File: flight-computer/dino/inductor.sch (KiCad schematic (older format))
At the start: 3 parts

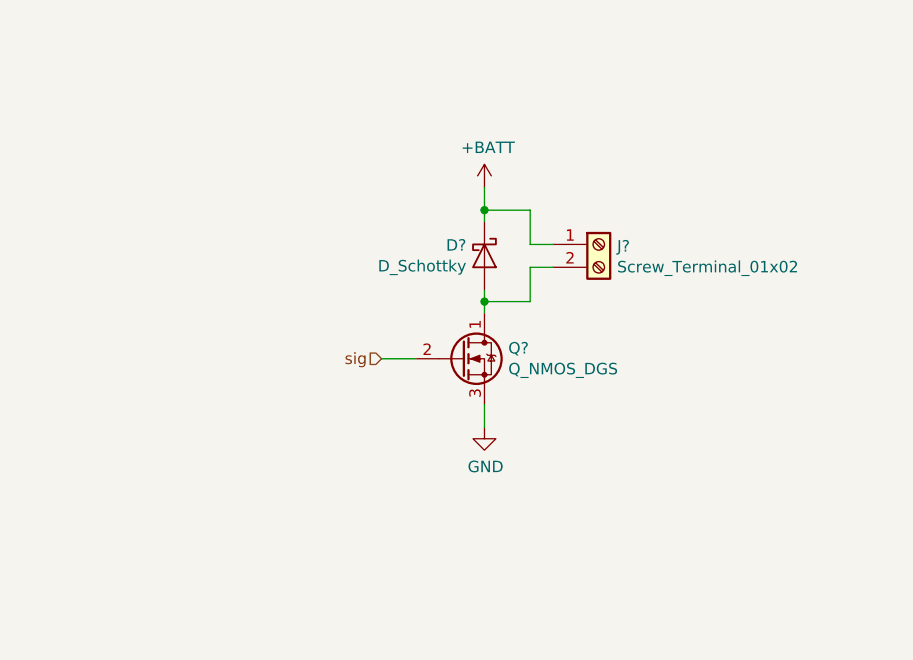
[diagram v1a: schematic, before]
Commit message: fc schematic fleshing-out and mcu docs
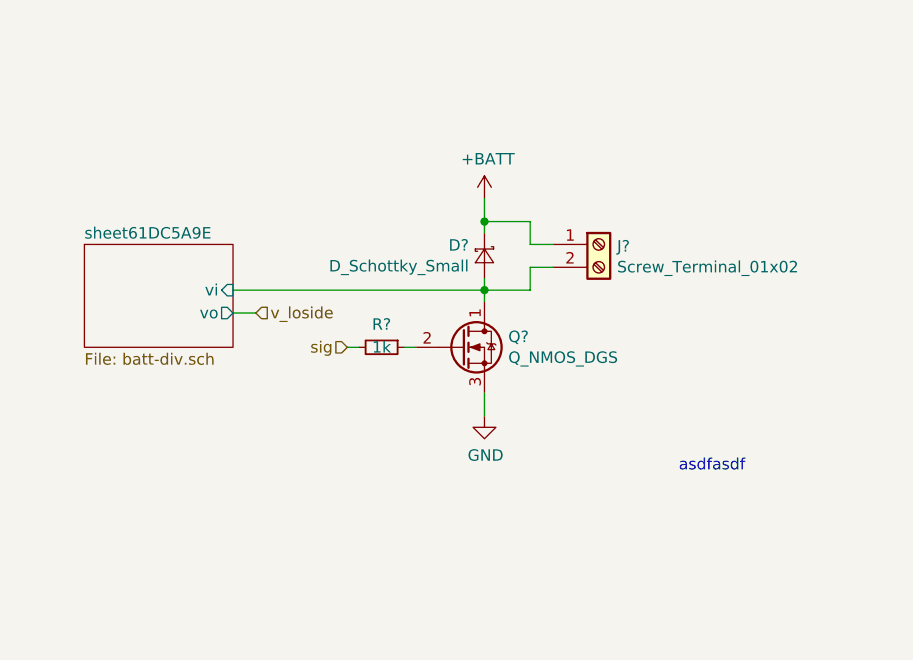
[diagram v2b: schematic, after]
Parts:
- removed D?: D_Schottky, symbol Device:D_Schottky
- added D?: D_Schottky_Small, symbol Device:D_Schottky_Small
- added R?: 1k, symbol Device:R_Small
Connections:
- net +BATT: now also D?.1 (K)
- net sig: now also R?.2; no longer Q?.2 (G)
- net sheet61DC5A9E/vi: now reaches J?.2 (Pin_2), Q?.1 (D)
- net sheet61DC5A9E/vi: now also D?.2 (A)
- new net: Q?.2 (G), R?.1
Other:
- note added: "asdfasdf"
- moved on the sheet: Q?
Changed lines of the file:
@@
 $Descr A 11000 8500
 encoding utf-8
-Sheet 2 8
+Sheet 10 14
 Title ""
 Date ""
@@
 L Device:Q_NMOS_DGS Q?
 U 1 1 61C15CF4
-P 5250 4600
+P 5250 4550
 AR Path="/61C15AA8/61C15CF4" Ref="Q?"  Part="1"
 AR Path="/61C229AC/61C15CF4" Ref="Q?"  Part="1"
 AR Path="/61C27E7D/61C15CF4" Ref="Q?"  Part="1"
 AR Path="/61C27F52/61C15CF4" Ref="Q?"  Part="1"
-F 0 "Q?" H 5454 4646 50  0000 L CNN
-F 1 "Q_NMOS_DGS" H 5454 4555 50  0000 L CNN
-F 2 "" H 5450 4700 50  0001 C CNN
-F 3 "~" H 5250 4600 50  0001 C CNN
-	1    5250 4600
+AR Path="/61D7382A/61C15CF4" Ref="Q?"  Part="1"
+F 0 "Q?" H 5454 4596 50  0000 L CNN
+F 1 "Q_NMOS_DGS" H 5454 4505 50  0000 L CNN
+F 2 "" H 5450 4650 50  0001 C CNN
+F 3 "~" H 5250 4550 50  0001 C CNN
+	1    5250 4550
 	1    0    0    -1
 $EndComp
@@
 L power:+BATT #PWR?
 U 1 1 61C163F4
-P 5350 3850
+P 5350 3900
 AR Path="/61C15AA8/61C163F4" Ref="#PWR?"  Part="1"
 AR Path="/61C229AC/61C163F4" Ref="#PWR?"  Part="1"
 AR Path="/61C27E7D/61C163F4" Ref="#PWR?"  Part="1"
 AR Path="/61C27F52/61C163F4" Ref="#PWR?"  Part="1"
-F 0 "#PWR?" H 5350 3700 50  0001 C CNN
-F 1 "+BATT" H 5365 4023 50  0000 C CNN
-F 2 "" H 5350 3850 50  0001 C CNN
-F 3 "" H 5350 3850 50  0001 C CNN
-	1    5350 3850
+AR Path="/61D7382A/61C163F4" Ref="#PWR?"  Part="1"
+F 0 "#PWR?" H 5350 3750 50  0001 C CNN
+F 1 "+BATT" H 5365 4073 50  0000 C CNN
+F 2 "" H 5350 3900 50  0001 C CNN
+F 3 "" H 5350 3900 50  0001 C CNN
+	1    5350 3900
 	1    0    0    -1
 $EndComp
@@
 L power:GND #PWR?
 U 1 1 61C16FAC
-P 5350 4900
+P 5350 4850
 AR Path="/61C15AA8/61C16FAC" Ref="#PWR?"  Part="1"
 AR Path="/61C229AC/61C16FAC" Ref="#PWR?"  Part="1"
 AR Path="/61C27E7D/61C16FAC" Ref="#PWR?"  Part="1"
 AR Path="/61C27F52/61C16FAC" Ref="#PWR?"  Part="1"
-F 0 "#PWR?" H 5350 4650 50  0001 C CNN
-F 1 "GND" H 5355 4727 50  0000 C CNN
-F 2 "" H 5350 4900 50  0001 C CNN
-F 3 "" H 5350 4900 50  0001 C CNN
-	1    5350 4900
+AR Path="/61D7382A/61C16FAC" Ref="#PWR?"  Part="1"
+F 0 "#PWR?" H 5350 4600 50  0001 C CNN
+F 1 "GND" H 5355 4677 50  0000 C CNN
+F 2 "" H 5350 4850 50  0001 C CNN
+F 3 "" H 5350 4850 50  0001 C CNN
+	1    5350 4850
 	1    0    0    -1
-$EndComp
-$Comp
-L Device:D_Schottky D?
-U 1 1 61C1778E
-P 5350 4150
-AR Path="/61C15AA8/61C1778E" Ref="D?"  Part="1"
-AR Path="/61C229AC/61C1778E" Ref="D?"  Part="1"
-AR Path="/61C27E7D/61C1778E" Ref="D?"  Part="1"
-AR Path="/61C27F52/61C1778E" Ref="D?"  Part="1"
-F 0 "D?" V 5304 4071 50  0000 R CNN
-F 1 "D_Schottky" V 5395 4071 50  0000 R CNN
-F 2 "" H 5350 4150 50  0001 C CNN
-F 3 "~" H 5350 4150 50  0001 C CNN
-	1    5350 4150
-	0    1    1    0
 $EndComp
 $Comp
@@
 AR Path="/61C27E7D/61C18064" Ref="J?"  Part="1"
 AR Path="/61C27F52/61C18064" Ref="J?"  Part="1"
+AR Path="/61D7382A/61C18064" Ref="J?"  Part="1"
 F 0 "J?" H 5930 4092 50  0000 L CNN
 F 1 "Screw_Terminal_01x02" H 5930 4001 50  0000 L CNN
@@
 $EndComp
 Wire Wire Line
-	5350 3850 5350 3950
+	5350 3900 5350 4000
 Wire Wire Line
 	5650 4100 5550 4100
 Wire Wire Line
-	5550 4100 5550 3950
+	5550 4000 5350 4000
+Connection ~ 5350 4000
 Wire Wire Line
-	5550 3950 5350 3950
-Connection ~ 5350 3950
+	5350 4000 5350 4050
 Wire Wire Line
-	5350 3950 5350 4000
+	5350 4250 5350 4300
+Wire Wire Line
+	5350 4300 5550 4300
+Wire Wire Line
+	5550 4300 5550 4200
+Wire Wire Line
+	5550 4200 5650 4200
+Connection ~ 5350 4300
 Wire Wire Line
 	5350 4300 5350 4350
 Wire Wire Line
-	5350 4350 5550 4350
+	5350 4750 5350 4850
+Text HLabel 4750 4550 0    50   Input ~ 0
+sig
+$Sheet
+S 3600 4100 650  450
+U 61DC5AA2
+F0 "sheet61DC5A9E" 50
+F1 "batt-div.sch" 50
+F2 "vo" O R 4250 4400 50
+F3 "vi" I R 4250 4300 50
+$EndSheet
 Wire Wire Line
-	5550 4350 5550 4200
+	5350 4300 4250 4300
 Wire Wire Line
-	5550 4200 5650 4200
-Connection ~ 5350 4350
+	4250 4400 4350 4400
+Text HLabel 4350 4400 2    50   Input ~ 0
+v_loside
+$Comp
+L Device:R_Small R?
+U 1 1 61DCB57D
+P 4900 4550
+AR Path="/61C27E7D/61DCB57D" Ref="R?"  Part="1"
+AR Path="/61C27F52/61DCB57D" Ref="R?"  Part="1"
+F 0 "R?" V 4800 4550 50  0000 C CNN
+F 1 "1k" V 4900 4550 50  0000 C CNN
+F 2 "" H 4900 4550 50  0001 C CNN
+F 3 "~" H 4900 4550 50  0001 C CNN
+	1    4900 4550
+	0    1    1    0
+$EndComp
+$Comp
+L Device:D_Schottky_Small D?
+U 1 1 61DCC192
+P 5350 4150
+AR Path="/61C27E7D/61DCC192" Ref="D?"  Part="1"
+AR Path="/61C27F52/61DCC192" Ref="D?"  Part="1"
+F 0 "D?" V 5304 4082 50  0000 R CNN
+F 1 "D_Schottky_Small" V 5395 4082 50  0000 R CNN
+F 2 "" V 5350 4150 50  0001 C CNN
+F 3 "~" V 5350 4150 50  0001 C CNN
+	1    5350 4150
+	0    1    1    0
+$EndComp
 Wire Wire Line
-	5350 4350 5350 4400
+	5550 4100 5550 4000
 Wire Wire Line
-	5350 4800 5350 4900
+	4750 4550 4800 4550
 Wire Wire Line
-	5050 4600 4900 4600
-Text HLabel 4900 4600 0    50   Input ~ 0
-sig
+	5000 4550 5050 4550
+Text Notes 6200 5100 0    50   ~ 0
+asdfasdf
 $EndSCHEMATC

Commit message: fc pinout and component selection. general cleanup
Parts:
- removed Q?: Q_NMOS_DGS, symbol Device:Q_NMOS_DGS
- added C?: 10u, Capacitor_Tantalum_SMD:CP_EIA-3216-18_Kemet-A, symbol Device:CP1
- added Q?: AO3400A, Package_TO_SOT_SMD:SOT-23, symbol Device:Q_NMOS_GSD
- added SW?: SW_SPDT, Connector_PinHeader_2.54mm:PinHeader_1x03_P2.54mm_Vertical, symbol Switch:SW_SPDT
- added TP? (x2): TestPoint, TestPoint:TestPoint_Keystone_5010-5014_Multipurpose, symbol Connector:TestPoint
- D?: value D_Schottky_Small -> 40V 5A 550mV; footprint (none) -> Diode_SMD:D_SMA; LCSC (none) -> C22452
- R?: footprint (none) -> Resistor_SMD:R_0603_1608Metric; LCSC (none) -> C21190
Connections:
- net labels added: v_hiside, v_sens_loside
- net labels removed: v_loside
- wire segments 15 -> 27
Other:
- note added: "LAYOUT: cap must be near connector"
- note added: "WARN: v_hiside can exceed 12V!"
- note added: "arming switch"
- note added: "decoupling cap"
- note removed: "asdfasdf"
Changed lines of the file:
@@
 $Descr A 11000 8500
 encoding utf-8
-Sheet 10 14
+Sheet 9 14
 Title ""
 Date ""
@@
 $EndDescr
 $Comp
-L Device:Q_NMOS_DGS Q?
-U 1 1 61C15CF4
-P 5250 4550
-AR Path="/61C15AA8/61C15CF4" Ref="Q?"  Part="1"
-AR Path="/61C229AC/61C15CF4" Ref="Q?"  Part="1"
-AR Path="/61C27E7D/61C15CF4" Ref="Q?"  Part="1"
-AR Path="/61C27F52/61C15CF4" Ref="Q?"  Part="1"
-AR Path="/61D7382A/61C15CF4" Ref="Q?"  Part="1"
-F 0 "Q?" H 5454 4596 50  0000 L CNN
-F 1 "Q_NMOS_DGS" H 5454 4505 50  0000 L CNN
-F 2 "" H 5450 4650 50  0001 C CNN
-F 3 "~" H 5250 4550 50  0001 C CNN
-	1    5250 4550
-	1    0    0    -1
-$EndComp
-$Comp
 L power:+BATT #PWR?
 U 1 1 61C163F4
-P 5350 3900
+P 5250 3450
 AR Path="/61C15AA8/61C163F4" Ref="#PWR?"  Part="1"
 AR Path="/61C229AC/61C163F4" Ref="#PWR?"  Part="1"
@@
 AR Path="/61C27F52/61C163F4" Ref="#PWR?"  Part="1"
 AR Path="/61D7382A/61C163F4" Ref="#PWR?"  Part="1"
-F 0 "#PWR?" H 5350 3750 50  0001 C CNN
-F 1 "+BATT" H 5365 4073 50  0000 C CNN
-F 2 "" H 5350 3900 50  0001 C CNN
-F 3 "" H 5350 3900 50  0001 C CNN
-	1    5350 3900
+AR Path="/61F91E79/61C163F4" Ref="#PWR?"  Part="1"
+AR Path="/61F965DC/61C163F4" Ref="#PWR?"  Part="1"
+AR Path="/61F965E7/61C163F4" Ref="#PWR?"  Part="1"
+F 0 "#PWR?" H 5250 3300 50  0001 C CNN
+F 1 "+BATT" H 5265 3623 50  0000 C CNN
+F 2 "" H 5250 3450 50  0001 C CNN
+F 3 "" H 5250 3450 50  0001 C CNN
+	1    5250 3450
 	1    0    0    -1
 $EndComp
@@
 AR Path="/61C27F52/61C16FAC" Ref="#PWR?"  Part="1"
 AR Path="/61D7382A/61C16FAC" Ref="#PWR?"  Part="1"
+AR Path="/61F91E79/61C16FAC" Ref="#PWR?"  Part="1"
+AR Path="/61F965DC/61C16FAC" Ref="#PWR?"  Part="1"
+AR Path="/61F965E7/61C16FAC" Ref="#PWR?"  Part="1"
 F 0 "#PWR?" H 5350 4600 50  0001 C CNN
 F 1 "GND" H 5355 4677 50  0000 C CNN
@@
 AR Path="/61C27F52/61C18064" Ref="J?"  Part="1"
 AR Path="/61D7382A/61C18064" Ref="J?"  Part="1"
+AR Path="/61F91E79/61C18064" Ref="J?"  Part="1"
+AR Path="/61F965DC/61C18064" Ref="J?"  Part="1"
+AR Path="/61F965E7/61C18064" Ref="J?"  Part="1"
 F 0 "J?" H 5930 4092 50  0000 L CNN
 F 1 "Screw_Terminal_01x02" H 5930 4001 50  0000 L CNN
@@
 $EndComp
 Wire Wire Line
-	5350 3900 5350 4000
-Wire Wire Line
 	5650 4100 5550 4100
 Wire Wire Line
@@
 Wire Wire Line
 	5350 4750 5350 4850
-Text HLabel 4750 4550 0    50   Input ~ 0
+Text HLabel 4700 4550 0    50   Input ~ 0
 sig
 $Sheet
@@
 	5350 4300 4250 4300
 Wire Wire Line
-	4250 4400 4350 4400
+	4250 4400 4300 4400
 Text HLabel 4350 4400 2    50   Input ~ 0
-v_loside
+v_sens_loside
 $Comp
 L Device:R_Small R?
@@
 AR Path="/61C27E7D/61DCB57D" Ref="R?"  Part="1"
 AR Path="/61C27F52/61DCB57D" Ref="R?"  Part="1"
+AR Path="/61C15AA8/61DCB57D" Ref="R?"  Part="1"
+AR Path="/61F91E79/61DCB57D" Ref="R?"  Part="1"
+AR Path="/61F965DC/61DCB57D" Ref="R?"  Part="1"
+AR Path="/61F965E7/61DCB57D" Ref="R?"  Part="1"
 F 0 "R?" V 4800 4550 50  0000 C CNN
 F 1 "1k" V 4900 4550 50  0000 C CNN
-F 2 "" H 4900 4550 50  0001 C CNN
+F 2 "Resistor_SMD:R_0603_1608Metric" H 4900 4550 50  0001 C CNN
 F 3 "~" H 4900 4550 50  0001 C CNN
+F 4 "C21190" V 4900 4550 50  0001 C CNN "LCSC"
 	1    4900 4550
 	0    1    1    0
@@
 AR Path="/61C27E7D/61DCC192" Ref="D?"  Part="1"
 AR Path="/61C27F52/61DCC192" Ref="D?"  Part="1"
+AR Path="/61C15AA8/61DCC192" Ref="D?"  Part="1"
+AR Path="/61F91E79/61DCC192" Ref="D?"  Part="1"
+AR Path="/61F965DC/61DCC192" Ref="D?"  Part="1"
+AR Path="/61F965E7/61DCC192" Ref="D?"  Part="1"
 F 0 "D?" V 5304 4082 50  0000 R CNN
-F 1 "D_Schottky_Small" V 5395 4082 50  0000 R CNN
-F 2 "" V 5350 4150 50  0001 C CNN
-F 3 "~" V 5350 4150 50  0001 C CNN
+F 1 "40V 5A 550mV" V 5395 4082 50  0000 R CNN
+F 2 "Diode_SMD:D_SMA" V 5350 4150 50  0001 C CNN
+F 3 "https://datasheet.lcsc.com/lcsc/1810192041_MDD%EF%BC%88Microdiode-Electronics%EF%BC%89-SS54_C22452.pdf" V 5350 4150 50  0001 C CNN
+F 4 "C22452" V 5350 4150 50  0001 C CNN "LCSC"
 	1    5350 4150
 	0    1    1    0
@@
 Wire Wire Line
 	5000 4550 5050 4550
-Text Notes 6200 5100 0    50   ~ 0
-asdfasdf
+$Comp
+L Device:Q_NMOS_GSD Q?
+U 1 1 61E3754D
+P 5250 4550
+AR Path="/61C27F52/61E3754D" Ref="Q?"  Part="1"
+AR Path="/61C15AA8/61E3754D" Ref="Q?"  Part="1"
+AR Path="/61C27E7D/61E3754D" Ref="Q?"  Part="1"
+AR Path="/61F91E79/61E3754D" Ref="Q?"  Part="1"
+AR Path="/61F965DC/61E3754D" Ref="Q?"  Part="1"
+AR Path="/61F965E7/61E3754D" Ref="Q?"  Part="1"
+F 0 "Q?" H 5455 4596 50  0000 L CNN
+F 1 "AO3400A" H 5455 4505 50  0000 L CNN
+F 2 "Package_TO_SOT_SMD:SOT-23" H 5450 4650 50  0001 C CNN
+F 3 "https://datasheet.lcsc.com/lcsc/1811081213_Alpha-&-Omega-Semicon-AO3400A_C20917.pdf" H 5250 4550 50  0001 C CNN
+	1    5250 4550
+	1    0    0    -1
+$EndComp
+$Comp
+L power:+BATT #PWR?
+U 1 1 61E403DE
+P 3900 5050
+AR Path="/61C229AC/61E403DE" Ref="#PWR?"  Part="1"
+AR Path="/61C267AB/61E403DE" Ref="#PWR?"  Part="1"
+AR Path="/61C3727F/61E403DE" Ref="#PWR?"  Part="1"
+AR Path="/61C37282/61E403DE" Ref="#PWR?"  Part="1"
+AR Path="/61DB5304/61E403DE" Ref="#PWR?"  Part="1"
+AR Path="/61C15AA8/61E403DE" Ref="#PWR?"  Part="1"
+AR Path="/61C27F52/61E403DE" Ref="#PWR?"  Part="1"
+AR Path="/61C27E7D/61E403DE" Ref="#PWR?"  Part="1"
+AR Path="/61F91E79/61E403DE" Ref="#PWR?"  Part="1"
+AR Path="/61F965DC/61E403DE" Ref="#PWR?"  Part="1"
+AR Path="/61F965E7/61E403DE" Ref="#PWR?"  Part="1"
+F 0 "#PWR?" H 3900 4900 50  0001 C CNN
+F 1 "+BATT" H 3915 5223 50  0000 C CNN
+F 2 "" H 3900 5050 50  0001 C CNN
+F 3 "" H 3900 5050 50  0001 C CNN
+	1    3900 5050
+	1    0    0    -1
+$EndComp
+$Comp
+L power:GND #PWR?
+U 1 1 61E403EA
+P 3900 5450
+AR Path="/61C229AC/61E403EA" Ref="#PWR?"  Part="1"
+AR Path="/61C15AA8/61E403EA" Ref="#PWR?"  Part="1"
+AR Path="/61C27F52/61E403EA" Ref="#PWR?"  Part="1"
+AR Path="/61C27E7D/61E403EA" Ref="#PWR?"  Part="1"
+AR Path="/61F91E79/61E403EA" Ref="#PWR?"  Part="1"
+AR Path="/61F965DC/61E403EA" Ref="#PWR?"  Part="1"
+AR Path="/61F965E7/61E403EA" Ref="#PWR?"  Part="1"
+F 0 "#PWR?" H 3900 5200 50  0001 C CNN
+F 1 "GND" H 3905 5277 50  0000 C CNN
+F 2 "" H 3900 5450 50  0001 C CNN
+F 3 "" H 3900 5450 50  0001 C CNN
+	1    3900 5450
+	1    0    0    -1
+$EndComp
+Wire Wire Line
+	3900 5450 3900 5400
+Wire Wire Line
+	3900 5100 3900 5050
+Text Notes 3650 5750 0    50   ~ 0
+decoupling cap
+$Comp
+L Switch:SW_SPDT SW?
+U 1 1 61E69DDA
+P 5350 3700
+AR Path="/61C27E7D/61E69DDA" Ref="SW?"  Part="1"
+AR Path="/61C27F52/61E69DDA" Ref="SW?"  Part="1"
+AR Path="/61F91E79/61E69DDA" Ref="SW?"  Part="1"
+AR Path="/61F965DC/61E69DDA" Ref="SW?"  Part="1"
+AR Path="/61F965E7/61E69DDA" Ref="SW?"  Part="1"
+F 0 "SW?" V 5396 3512 50  0000 R CNN
+F 1 "SW_SPDT" V 5305 3512 50  0000 R CNN
+F 2 "Connector_PinHeader_2.54mm:PinHeader_1x03_P2.54mm_Vertical" H 5350 3700 50  0001 C CNN
+F 3 "~" H 5350 3700 50  0001 C CNN
+	1    5350 3700
+	0    -1   -1   0
+$EndComp
+Wire Wire Line
+	5250 3450 5250 3500
+Text Notes 5650 3550 0    50   ~ 0
+arming switch
+Wire Wire Line
+	5350 3900 5350 4000
+Text HLabel 5200 4000 0    50   Input ~ 0
+v_hiside
+Wire Wire Line
+	5200 4000 5350 4000
+Text Notes 3750 3650 0    50   ~ 0
+WARN: v_hiside can exceed 12V!
+$Comp
+L Connector:TestPoint TP?
+U 1 1 61E7CEBE
+P 4900 4800
+AR Path="/61C229AC/61E7CEBE" Ref="TP?"  Part="1"
+AR Path="/61C27E7D/61E7CEBE" Ref="TP?"  Part="1"
+AR Path="/61C27F52/61E7CEBE" Ref="TP?"  Part="1"
+AR Path="/61F91E79/61E7CEBE" Ref="TP?"  Part="1"
+AR Path="/61F965DC/61E7CEBE" Ref="TP?"  Part="1"
+AR Path="/61F965E7/61E7CEBE" Ref="TP?"  Part="1"
+F 0 "TP?" H 4958 4918 50  0000 L CNN
+F 1 "TestPoint" H 4958 4827 50  0000 L CNN
+F 2 "TestPoint:TestPoint_Keystone_5010-5014_Multipurpose" H 5100 4800 50  0001 C CNN
+F 3 "~" H 5100 4800 50  0001 C CNN
+	1    4900 4800
+	-1   0    0    1
+$EndComp
+Wire Wire Line
+	4900 4800 4900 4700
+Wire Wire Line
+	4900 4700 4750 4700
+Wire Wire Line
+	4750 4700 4750 4550
+Wire Wire Line
+	4750 4550 4700 4550
+Connection ~ 4750 4550
+$Comp
+L Connector:TestPoint TP?
+U 1 1 61E7E697
+P 4400 4800
+AR Path="/61C229AC/61E7E697" Ref="TP?"  Part="1"
+AR Path="/61C27E7D/61E7E697" Ref="TP?"  Part="1"
+AR Path="/61C27F52/61E7E697" Ref="TP?"  Part="1"
+AR Path="/61F91E79/61E7E697" Ref="TP?"  Part="1"
+AR Path="/61F965DC/61E7E697" Ref="TP?"  Part="1"
+AR Path="/61F965E7/61E7E697" Ref="TP?"  Part="1"
+F 0 "TP?" H 4458 4918 50  0000 L CNN
+F 1 "TestPoint" H 4458 4827 50  0000 L CNN
+F 2 "TestPoint:TestPoint_Keystone_5010-5014_Multipurpose" H 4600 4800 50  0001 C CNN
+F 3 "~" H 4600 4800 50  0001 C CNN
+	1    4400 4800
+	-1   0    0    1
+$EndComp
+Wire Wire Line
+	4400 4800 4400 4550
+Wire Wire Line
+	4400 4550 4300 4550
+Wire Wire Line
+	4300 4550 4300 4400
+Connection ~ 4300 4400
+Wire Wire Line
+	4300 4400 4350 4400
+$Comp
+L Device:CP1 C?
+U 1 1 61F12425
+P 3900 5250
+AR Path="/61F12425" Ref="C?"  Part="1"
+AR Path="/61C27E7D/61F12425" Ref="C?"  Part="1"
+AR Path="/61F91E79/61F12425" Ref="C?"  Part="1"
+AR Path="/61F965DC/61F12425" Ref="C?"  Part="1"
+AR Path="/61F965E7/61F12425" Ref="C?"  Part="1"
+F 0 "C?" H 4015 5296 50  0000 L CNN
+F 1 "10u" H 4015 5205 50  0000 L CNN
+F 2 "Capacitor_Tantalum_SMD:CP_EIA-3216-18_Kemet-A" H 3900 5250 50  0001 C CNN
+F 3 "https://datasheet.lcsc.com/lcsc/1811071223_AVX-TAJA106K016RNJ_C7171.pdf" H 3900 5250 50  0001 C CNN
+F 4 "C7171" H 3900 5250 50  0001 C CNN "LCSC"
+	1    3900 5250
+	1    0    0    -1
+$EndComp
+Text Notes 5450 5700 0    50   ~ 10
+LAYOUT: cap must be near connector
 $EndSCHEMATC
